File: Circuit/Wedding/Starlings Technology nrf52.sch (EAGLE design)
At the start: 22 parts, among them IC1 MCP1703CB, J7 CORTEX_DEBUG_SMD, U3 BC840M, U5 74AHCT2G125, Y2 FC-12M

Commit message: Tinier size board, with new external buttons and switch.
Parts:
- removed POWER_IN: (no value), SparkFun-Connectors:JST_2MM_MALE
- removed S1: CF-LD-1DC4-AR2W, RA1122DWR:CF-LD-1DC4-AR2W
- added J2: (no value), SparkFun-Connectors:CONN_02LOCK_LONGPADS
- added S4: (no value), SparkFun-Switches:SWITCH-SPDT-PTH-11.6X4.0MM
- S2, S3: device SparkFun-Switches:MOMENTARY-SWITCH-SPST-PTH-6.0MM -> adafruit:SWITCH_PUSHBUTTONEVQ-PE
- U3: DIGIKEY 1914-BC840MCT-ND -> 1914-BC840CT-ND
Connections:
- removed net N$4: C20.1, IC1.VI
- net GND: now also J2.2, S2.P$1, S3.P$1; no longer POWER_IN.-, S2.1, S3.1
- net SWITCH_1: now also S3.P$2; no longer S3.2
- net SWITCH_2: now also S2.P$2; no longer S2.2
- net VBAT: now also C20.1, IC1.VI, S4.O; no longer S1.4
- net VBAT_RAW: now also J2.1, S4.P; no longer POWER_IN.+, S1.5
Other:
- moved on the sheet: IC1

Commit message: Finalizing board, switched all connectors to wide pads.
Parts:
- removed C17, C9: 22pF, SparkFun-Capacitors:22UF-0805-6.3V-20%
- removed S2, S3: TL1105, adafruit:SWITCH_PUSHBUTTONEVQ-PE
- removed S4: (no value), SparkFun-Switches:SWITCH-SPDT-PTH-11.6X4.0MM
- removed Y2: FC-12M, crystal:FC-12M
- added J3, J4, J5: (no value), SparkFun-Connectors:CONN_02LOCK_LONGPADS
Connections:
- removed net N$17: C17.1, U3.F6/P000, Y2.2
- removed net N$2: C9.1, U3.F7/P001, Y2.1
- net GND: now also J3.1, J4.1; no longer C17.2, C9.2, S2.P$1, S3.P$1
- net SWITCH_1: now also J3.2; no longer S3.P$2
- net SWITCH_2: now also J4.2; no longer S2.P$2
- net VBAT: now also J5.1; no longer S4.O
- net VBAT_RAW: now also J5.2; no longer S4.P

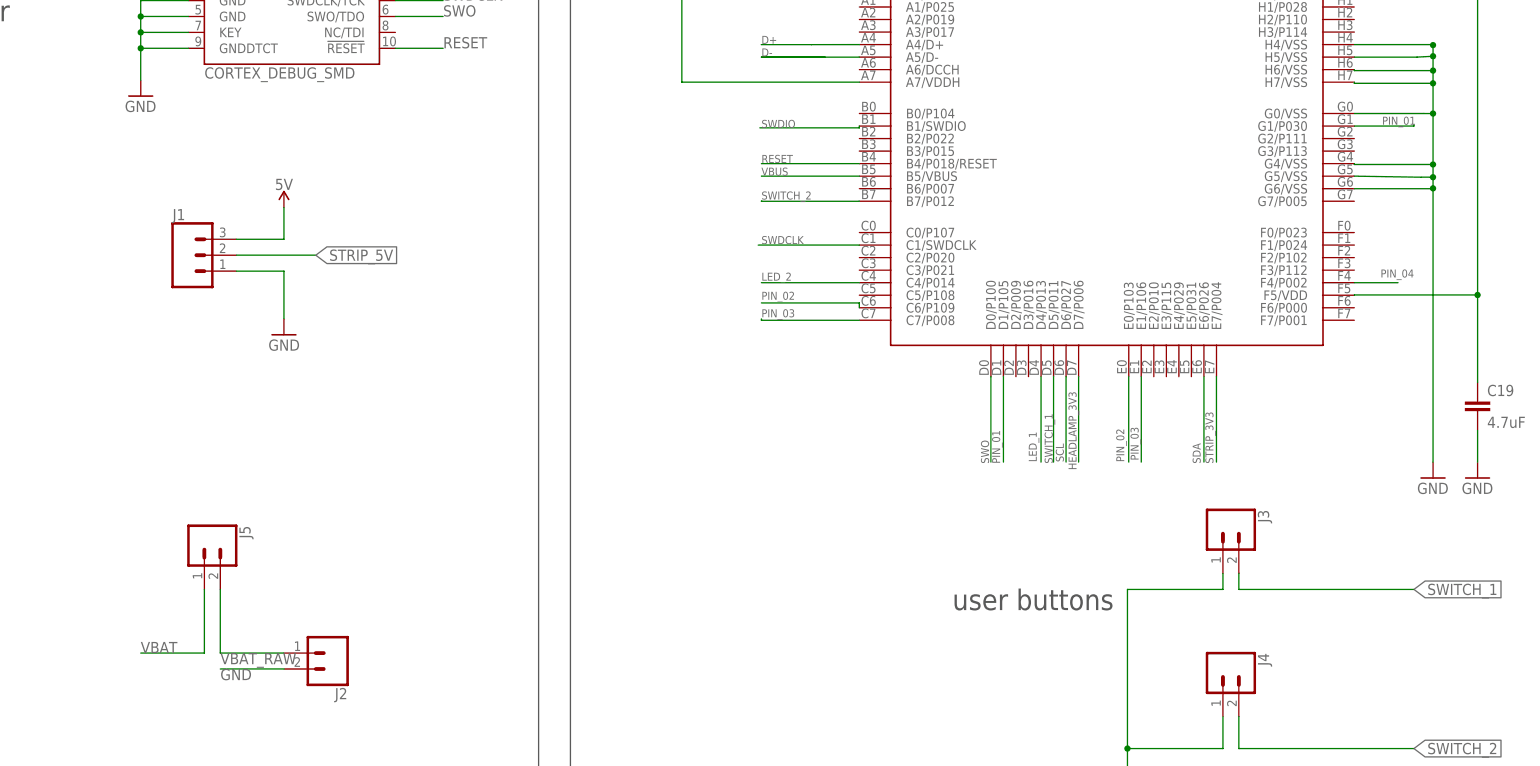
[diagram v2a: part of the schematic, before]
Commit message: Rev 2 of the wedding swarm board. Connected 5V and VBAT lines. Embiggened switches.
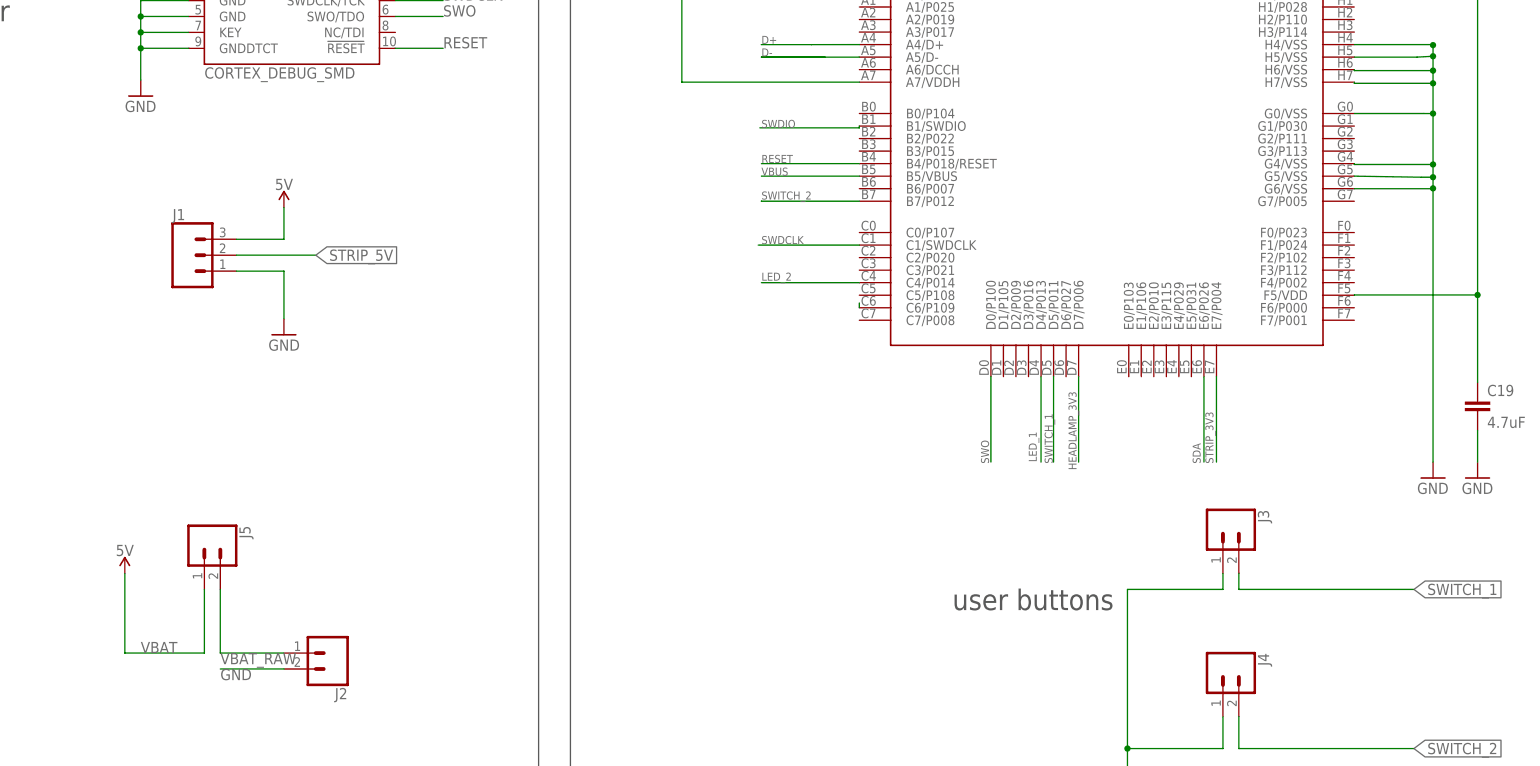
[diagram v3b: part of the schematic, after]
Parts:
- J2: DIGIKEY (none) -> S1111EC-02-ND
- J3, J4, J5: device SparkFun-Connectors:CONN_02LOCK_LONGPADS -> SparkFun-Connectors:CONN_02PTH4
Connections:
- removed net 5V: J1.3, U5.8
- removed net PIN_01: U3.D1/P105, U3.G1/P030
- removed net PIN_03: U3.C7/P008, U3.E1/P106
- removed net PIN_04: U3.F4/P002
- removed net SCL: U3.D6/P027
- net PIN_02: no longer U3.E0/P103
- net VBAT: now also J1.3, U5.8
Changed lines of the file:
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@@
 <attribute name="DIGIKEY" value="RNCP0603FTD1K00CT-ND"/>
 </part>
-<part name="J2" library="SparkFun-Connectors" library_urn="urn:adsk.eagle:library:513" deviceset="CONN_02" device="LOCK_LONGPADS" package3d_urn="urn:adsk.eagle:package:38047/1"/>
-<part name="J3" library="SparkFun-Connectors" library_urn="urn:adsk.eagle:library:513" deviceset="CONN_02" device="LOCK_LONGPADS" package3d_urn="urn:adsk.eagle:package:38047/1"/>
-<part name="J4" library="SparkFun-Connectors" library_urn="urn:adsk.eagle:library:513" deviceset="CONN_02" device="LOCK_LONGPADS" package3d_urn="urn:adsk.eagle:package:38047/1"/>
-<part name="J5" library="SparkFun-Connectors" library_urn="urn:adsk.eagle:library:513" deviceset="CONN_02" device="LOCK_LONGPADS" package3d_urn="urn:adsk.eagle:package:38047/1"/>
+<part name="J2" library="SparkFun-Connectors" library_urn="urn:adsk.eagle:library:513" deviceset="CONN_02" device="LOCK_LONGPADS" package3d_urn="urn:adsk.eagle:package:38047/1">
+<attribute name="DIGIKEY" value="S1111EC-02-ND"/>
+</part>
+<part name="J3" library="SparkFun-Connectors" library_urn="urn:adsk.eagle:library:513" deviceset="CONN_02" device="PTH4" package3d_urn="urn:adsk.eagle:package:38054/1"/>
+<part name="J4" library="SparkFun-Connectors" library_urn="urn:adsk.eagle:library:513" deviceset="CONN_02" device="PTH4" package3d_urn="urn:adsk.eagle:package:38054/1"/>
+<part name="J5" library="SparkFun-Connectors" library_urn="urn:adsk.eagle:library:513" deviceset="CONN_02" device="PTH4" package3d_urn="urn:adsk.eagle:package:38054/1"/>
+<part name="P+1" library="SparkFun-PowerSymbols" deviceset="VCC" device="" value="5V"/>
 </parts>
 <sheets>
@@
 <attribute name="VALUE" x="-35.56" y="58.166" size="1.778" layer="96" font="vector" rot="R180"/>
 <attribute name="NAME" x="-35.56" y="47.752" size="1.778" layer="95" font="vector" rot="R180"/>
+<attribute name="DIGIKEY" x="-38.1" y="53.34" size="1.778" layer="96" rot="R180" display="off"/>
 </instance>
 <instance part="J3" gate="G$1" x="104.14" y="73.66" smashed="yes" rot="R270">
@@
 <attribute name="VALUE" x="-63.246" y="73.66" size="1.778" layer="96" font="vector" rot="R270"/>
 <attribute name="NAME" x="-52.832" y="73.66" size="1.778" layer="95" font="vector" rot="R270"/>
+</instance>
+<instance part="P+1" gate="G$1" x="-71.12" y="66.04" smashed="yes" rot="MR0">
+<attribute name="VALUE" x="-71.12" y="68.834" size="1.778" layer="96" rot="MR0" align="bottom-center"/>
 </instance>
 </instances>
@@
 </segment>
 </net>
-<net name="5V" class="0">
-<segment>
-<wire x1="441.96" y1="35.56" x2="452.12" y2="35.56" width="0.1524" layer="91"/>
-<pinref part="P+3" gate="1" pin="VCC"/>
-<pinref part="U5" gate="A" pin="8"/>
-</segment>
-<segment>
-<wire x1="-53.34" y1="119.38" x2="-45.72" y2="119.38" width="0.1524" layer="91"/>
-<pinref part="P+10" gate="G$1" pin="VCC"/>
-<wire x1="-45.72" y1="119.38" x2="-45.72" y2="124.46" width="0.1524" layer="91"/>
-<pinref part="J1" gate="J$1" pin="3"/>
-</segment>
-</net>
 <net name="STRIP_3V3" class="0">
 <segment>
@@
 </segment>
 </net>
-<net name="VBAT" class="0">
-<segment>
-<pinref part="P+12" gate="G$1" pin="3.3V"/>
-<pinref part="C20" gate="G$1" pin="1"/>
-<wire x1="279.4" y1="30.48" x2="279.4" y2="22.86" width="0.1524" layer="91"/>
-<junction x="279.4" y="30.48"/>
-<wire x1="279.4" y1="30.48" x2="302.26" y2="30.48" width="0.1524" layer="91"/>
-<pinref part="IC1" gate="G$1" pin="VI"/>
-<wire x1="279.4" y1="40.64" x2="279.4" y2="30.48" width="0.1524" layer="91"/>
-</segment>
-<segment>
-<pinref part="J5" gate="G$1" pin="1"/>
-<wire x1="-58.42" y1="63.5" x2="-58.42" y2="53.34" width="0.1524" layer="91"/>
-<wire x1="-58.42" y1="53.34" x2="-68.58" y2="53.34" width="0.1524" layer="91"/>
-<label x="-68.58" y="53.34" size="1.778" layer="95"/>
-</segment>
-</net>
 <net name="VBAT_RAW" class="0">
 <segment>
@@
 </segment>
 </net>
-<net name="SCL" class="0">
-<segment>
-<pinref part="U3" gate="G$1" pin="D6/P027"/>
-<wire x1="79.106" y1="97.454" x2="79.106" y2="83.82" width="0.1524" layer="91"/>
-<label x="78.74" y="83.82" size="1.27" layer="95" rot="R90"/>
-</segment>
-</net>
-<net name="PIN_01" class="0">
-<segment>
-<pinref part="U3" gate="G$1" pin="D1/P105"/>
-<wire x1="69.106" y1="97.454" x2="69.106" y2="83.82" width="0.1524" layer="91"/>
-<label x="68.58" y="83.566" size="1.27" layer="95" rot="R90"/>
-</segment>
-<segment>
-<pinref part="U3" gate="G$1" pin="G1/P030"/>
-<wire x1="125.106" y1="137.454" x2="134.62" y2="137.454" width="0.1524" layer="91"/>
-<wire x1="134.62" y1="137.454" x2="134.62" y2="137.668" width="0.1524" layer="91"/>
-<label x="129.54" y="137.668" size="1.27" layer="95"/>
-</segment>
-</net>
 <net name="PIN_02" class="0">
-<segment>
-<pinref part="U3" gate="G$1" pin="E0/P103"/>
-<wire x1="89.106" y1="97.454" x2="89.106" y2="83.82" width="0.1524" layer="91"/>
-<label x="88.392" y="83.82" size="1.27" layer="95" rot="R90"/>
-</segment>
 <segment>
 <pinref part="U3" gate="G$1" pin="C6/P109"/>
 <wire x1="46.106" y1="108.454" x2="46.106" y2="109.22" width="0.1524" layer="91"/>
-<wire x1="46.106" y1="109.22" x2="30.48" y2="109.22" width="0.1524" layer="91"/>
-<label x="30.48" y="109.728" size="1.27" layer="95"/>
-</segment>
-</net>
-<net name="PIN_03" class="0">
-<segment>
-<pinref part="U3" gate="G$1" pin="E1/P106"/>
-<wire x1="91.106" y1="97.454" x2="91.106" y2="83.82" width="0.1524" layer="91"/>
-<label x="90.678" y="84.074" size="1.27" layer="95" rot="R90"/>
-</segment>
-<segment>
-<pinref part="U3" gate="G$1" pin="C7/P008"/>
-<wire x1="46.106" y1="106.454" x2="30.48" y2="106.454" width="0.1524" layer="91"/>
-<wire x1="30.48" y1="106.454" x2="30.48" y2="106.68" width="0.1524" layer="91"/>
-<label x="30.48" y="106.934" size="1.27" layer="95"/>
-</segment>
-</net>
-<net name="PIN_04" class="0">
-<segment>
-<pinref part="U3" gate="G$1" pin="F4/P002"/>
-<wire x1="125.106" y1="112.454" x2="132.08" y2="112.454" width="0.1524" layer="91"/>
-<label x="129.286" y="113.284" size="1.27" layer="95"/>
 </segment>
 </net>
@@
 </segment>
 </net>
+<net name="VBAT" class="0">
+<segment>
+<pinref part="J5" gate="G$1" pin="1"/>
+<wire x1="-58.42" y1="63.5" x2="-58.42" y2="53.34" width="0.1524" layer="91"/>
+<wire x1="-58.42" y1="53.34" x2="-71.12" y2="53.34" width="0.1524" layer="91"/>
+<label x="-68.58" y="53.34" size="1.778" layer="95"/>
+<wire x1="-71.12" y1="53.34" x2="-71.12" y2="66.04" width="0.1524" layer="91"/>
+<pinref part="P+1" gate="G$1" pin="VCC"/>
+</segment>
+<segment>
+<pinref part="P+12" gate="G$1" pin="3.3V"/>
+<pinref part="C20" gate="G$1" pin="1"/>
+<wire x1="279.4" y1="30.48" x2="279.4" y2="22.86" width="0.1524" layer="91"/>
+<junction x="279.4" y="30.48"/>
+<wire x1="279.4" y1="30.48" x2="302.26" y2="30.48" width="0.1524" layer="91"/>
+<pinref part="IC1" gate="G$1" pin="VI"/>
+<wire x1="279.4" y1="40.64" x2="279.4" y2="30.48" width="0.1524" layer="91"/>
+</segment>
+<segment>
+<wire x1="441.96" y1="35.56" x2="452.12" y2="35.56" width="0.1524" layer="91"/>
+<pinref part="P+3" gate="1" pin="VCC"/>
+<pinref part="U5" gate="A" pin="8"/>
+</segment>
+<segment>
+<wire x1="-53.34" y1="119.38" x2="-45.72" y2="119.38" width="0.1524" layer="91"/>
+<pinref part="P+10" gate="G$1" pin="VCC"/>
+<wire x1="-45.72" y1="119.38" x2="-45.72" y2="124.46" width="0.1524" layer="91"/>
+<pinref part="J1" gate="J$1" pin="3"/>
+</segment>
+</net>
